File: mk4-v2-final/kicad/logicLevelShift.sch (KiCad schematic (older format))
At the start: 3 parts

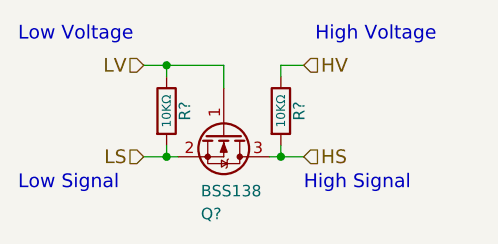
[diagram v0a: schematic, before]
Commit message: added headnight diodes, I don't think software control of them is going to be possible
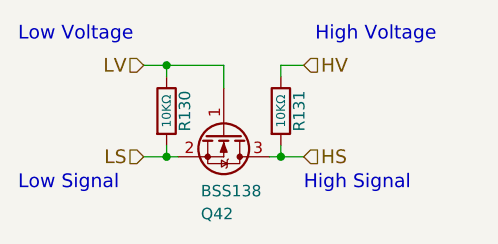
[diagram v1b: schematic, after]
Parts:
- gave numbers to parts that had none: 3
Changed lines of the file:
@@
 $EndDescr
 $Comp
-L BSS138 Q?
+L BSS138 Q41
 U 1 1 5B217257
 P 6350 4000
-AR Path="/59DEA30F/5B2166FB/5B217257" Ref="Q?"  Part="1"
-AR Path="/59DEA30F/5B235833/5B217257" Ref="Q?"  Part="1"
-F 0 "Q?" V 6700 3900 50  0000 L CNN
+AR Path="/59DEA30F/5B2166FB/5B217257" Ref="Q41"  Part="1"
+AR Path="/59DEA30F/5B235833/5B217257" Ref="Q42"  Part="1"
+F 0 "Q42" V 6700 3900 50  0000 L CNN
 F 1 "BSS138" V 6600 3900 50  0000 L CNN
 F 2 "TO_SOT_Packages_SMD:SOT-23" H 6550 3925 50  0001 L CIN
@@
 LV
 $Comp
-L R R?
+L R R128
 U 1 1 5B217274
 P 6100 3900
-AR Path="/59DEA30F/5B2166FB/5B217274" Ref="R?"  Part="1"
-AR Path="/59DEA30F/5B235833/5B217274" Ref="R?"  Part="1"
-F 0 "R?" V 6180 3900 50  0000 C CNN
+AR Path="/59DEA30F/5B2166FB/5B217274" Ref="R128"  Part="1"
+AR Path="/59DEA30F/5B235833/5B217274" Ref="R130"  Part="1"
+F 0 "R130" V 6180 3900 50  0000 C CNN
 F 1 "10KΩ" V 6100 3900 39  0000 C CNN
 F 2 "" V 6030 3900 50  0001 C CNN
@@
 	6000 3700 6350 3700
 $Comp
-L R R?
+L R R129
 U 1 1 5B21E775
 P 6600 3900
-AR Path="/59DEA30F/5B2166FB/5B21E775" Ref="R?"  Part="1"
-AR Path="/59DEA30F/5B235833/5B21E775" Ref="R?"  Part="1"
-F 0 "R?" V 6680 3900 50  0000 C CNN
+AR Path="/59DEA30F/5B2166FB/5B21E775" Ref="R129"  Part="1"
+AR Path="/59DEA30F/5B235833/5B21E775" Ref="R131"  Part="1"
+F 0 "R131" V 6680 3900 50  0000 C CNN
 F 1 "10KΩ" V 6600 3900 39  0000 C CNN
 F 2 "" V 6530 3900 50  0001 C CNN

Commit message: schematic is done, footprint association and netlist are also done
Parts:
- Q41: digikey-pn (none) -> BSS138LT1GOSCT-ND; mfg-pn (none) -> BSS138LT1G
- R128, R129: footprint (none) -> Resistors_THT:R_Axial_DIN0204_L3.6mm_D1.6mm_P5.08mm_Horizontal; digikey-pn (none) -> BC10.0KXCT-ND; mfg-pn (none) -> MBA02040C1002FRP00
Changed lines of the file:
@@
 EESchema Schematic File Version 2
-LIBS:hitchco-mk4-rescue
 LIBS:power
 LIBS:device
@@
 LIBS:cd4013b
 LIBS:ncs3s1205sc
+LIBS:lca715
+LIBS:SN74HC595N
+LIBS:CD74HC4067
 LIBS:hitchco-mk4-cache
 EELAYER 25 0
@@
 $Descr A4 11693 8268
 encoding utf-8
-Sheet 53 54
+Sheet 54 54
 Title ""
 Date ""
@@
 F 1 "BSS138" V 6600 3900 50  0000 L CNN
 F 2 "TO_SOT_Packages_SMD:SOT-23" H 6550 3925 50  0001 L CIN
-F 3 "" H 6350 4000 50  0001 L CNN
+F 3 "http://www.onsemi.com/pub/Collateral/BSS138LT1-D.PDF" H 6350 4000 50  0001 L CNN
+F 4 "BSS138LT1GOSCT-ND" V 6350 4000 60  0001 C CNN "digikey-pn"
+F 5 "BSS138LT1G" V 6350 4000 60  0001 C CNN "mfg-pn"
 	1    6350 4000
 	0    1    1    0
 $EndComp
-Text HLabel 6000 3700 0    60   Input ~ 0
-LV
 $Comp
 L R R128
@@
 F 0 "R130" V 6180 3900 50  0000 C CNN
 F 1 "10KΩ" V 6100 3900 39  0000 C CNN
-F 2 "" V 6030 3900 50  0001 C CNN
+F 2 "Resistors_THT:R_Axial_DIN0204_L3.6mm_D1.6mm_P5.08mm_Horizontal" V 6030 3900 50  0001 C CNN
 F 3 "" H 6100 3900 50  0001 C CNN
+F 4 "BC10.0KXCT-ND" H 6180 4000 50  0001 C CNN "digikey-pn"
+F 5 "MBA02040C1002FRP00" H 6180 4000 50  0001 C CNN "mfg-pn"
 	1    6100 3900
 	1    0    0    -1
 $EndComp
-Text HLabel 6000 4100 0    60   Input ~ 0
-LS
-Text HLabel 6700 4100 2    60   Input ~ 0
-HS
-Text HLabel 6700 3700 2    60   Input ~ 0
-HV
-Wire Wire Line
-	6350 3700 6350 3800
-Wire Wire Line
-	6100 3750 6100 3700
-Connection ~ 6100 3700
-Wire Wire Line
-	6100 4050 6100 4100
-Connection ~ 6100 4100
-Wire Wire Line
-	6000 4100 6150 4100
-Wire Wire Line
-	6000 3700 6350 3700
 $Comp
 L R R129
@@
 F 0 "R131" V 6680 3900 50  0000 C CNN
 F 1 "10KΩ" V 6600 3900 39  0000 C CNN
-F 2 "" V 6530 3900 50  0001 C CNN
+F 2 "Resistors_THT:R_Axial_DIN0204_L3.6mm_D1.6mm_P5.08mm_Horizontal" V 6530 3900 50  0001 C CNN
 F 3 "" H 6600 3900 50  0001 C CNN
+F 4 "BC10.0KXCT-ND" H 6680 4000 50  0001 C CNN "digikey-pn"
+F 5 "MBA02040C1002FRP00" H 6680 4000 50  0001 C CNN "mfg-pn"
 	1    6600 3900
 	1    0    0    -1
 $EndComp
-Wire Wire Line
-	6600 3700 6600 3750
-Wire Wire Line
-	6600 4100 6600 4050
-Connection ~ 6600 4100
-Wire Wire Line
-	6700 3700 6600 3700
-Wire Wire Line
-	6550 4100 6700 4100
+Text HLabel 6000 3700 0    60   Input ~ 0
+LV
+Text HLabel 6000 4100 0    60   Input ~ 0
+LS
+Text HLabel 6700 4100 2    60   Input ~ 0
+HS
+Text HLabel 6700 3700 2    60   Input ~ 0
+HV
 Text Notes 5450 3600 0    60   ~ 0
 Low Voltage
@@
 Text Notes 6700 4250 0    60   ~ 0
 High Signal
+Wire Wire Line
+	6350 3700 6350 3800
+Wire Wire Line
+	6100 3750 6100 3700
+Wire Wire Line
+	6100 4050 6100 4100
+Wire Wire Line
+	6000 4100 6150 4100
+Wire Wire Line
+	6000 3700 6350 3700
+Wire Wire Line
+	6600 3700 6600 3750
+Wire Wire Line
+	6600 4100 6600 4050
+Wire Wire Line
+	6700 3700 6600 3700
+Wire Wire Line
+	6550 4100 6700 4100
+Connection ~ 6100 3700
+Connection ~ 6100 4100
+Connection ~ 6600 4100
 $EndSCHEMATC

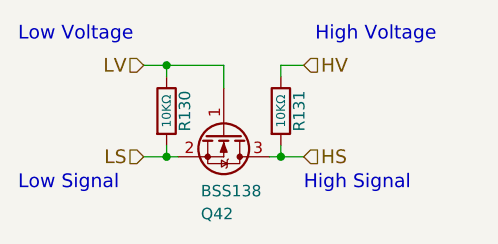
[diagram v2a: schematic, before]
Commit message: all components on the board
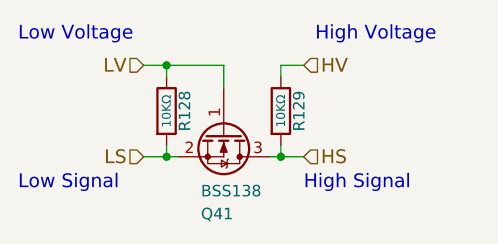
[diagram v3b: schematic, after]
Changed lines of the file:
@@
 AR Path="/59DEA30F/5B2166FB/5B217257" Ref="Q41"  Part="1"
 AR Path="/59DEA30F/5B235833/5B217257" Ref="Q42"  Part="1"
-F 0 "Q42" V 6700 3900 50  0000 L CNN
+F 0 "Q41" V 6700 3900 50  0000 L CNN
 F 1 "BSS138" V 6600 3900 50  0000 L CNN
 F 2 "TO_SOT_Packages_SMD:SOT-23" H 6550 3925 50  0001 L CIN
@@
 AR Path="/59DEA30F/5B2166FB/5B217274" Ref="R128"  Part="1"
 AR Path="/59DEA30F/5B235833/5B217274" Ref="R130"  Part="1"
-F 0 "R130" V 6180 3900 50  0000 C CNN
+F 0 "R128" V 6180 3900 50  0000 C CNN
 F 1 "10KΩ" V 6100 3900 39  0000 C CNN
 F 2 "Resistors_THT:R_Axial_DIN0204_L3.6mm_D1.6mm_P5.08mm_Horizontal" V 6030 3900 50  0001 C CNN
@@
 AR Path="/59DEA30F/5B2166FB/5B21E775" Ref="R129"  Part="1"
 AR Path="/59DEA30F/5B235833/5B21E775" Ref="R131"  Part="1"
-F 0 "R131" V 6680 3900 50  0000 C CNN
+F 0 "R129" V 6680 3900 50  0000 C CNN
 F 1 "10KΩ" V 6600 3900 39  0000 C CNN
 F 2 "Resistors_THT:R_Axial_DIN0204_L3.6mm_D1.6mm_P5.08mm_Horizontal" V 6530 3900 50  0001 C CNN
